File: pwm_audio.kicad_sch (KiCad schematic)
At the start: 16 parts, among them J4 PJ-320D, U7 NC7WZ16P6X

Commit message: Rev.2 (260322)
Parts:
- removed C23: 100n, Capacitor_SMD:C_0402_1005Metric, symbol Device:C
- removed U7: NC7WZ16P6X, Package_TO_SOT_SMD:SOT-363_SC-70-6, symbol 74xGxx:74LVC2G34
- C24, C25: value 100n -> 220n; LCSC (none) -> C21120
- C26, C27: LCSC (none) -> C16133
- D7: renamed from D4; LCSC (none) -> C20615784
- D8: renamed from D5; LCSC (none) -> C20615784
- J4: LCSC (none) -> C431535
- R28, R29: footprint Resistor_SMD:R_0402_1005Metric -> Resistor_SMD:R_0603_1608Metric; LCSC (none) -> C22962
- R30, R31: footprint Resistor_SMD:R_0402_1005Metric -> Resistor_SMD:R_0603_1608Metric; LCSC (none) -> C22775
- R32, R33: footprint Resistor_SMD:R_0402_1005Metric -> Resistor_SMD:R_0603_1608Metric; LCSC (none) -> C25804
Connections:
- net AUDIO_L: now also R28.1
- net AUDIO_R: now also R29.1
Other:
- moved on the sheet: C24, C25, C26, C27, D7, D8, J4, NT1, R28, R29, R30, R31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

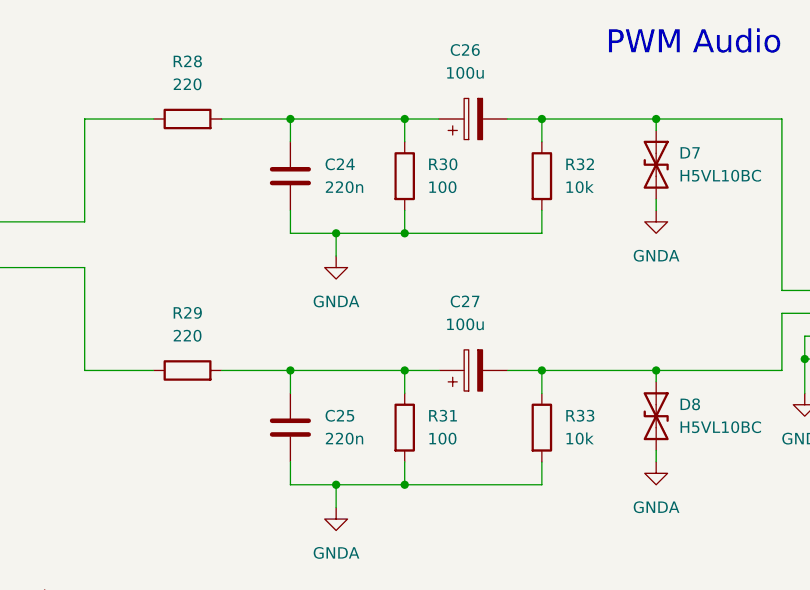
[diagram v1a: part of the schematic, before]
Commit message: Rev. 2B: Change PSRAM package from SOP-8 to USON-8L.
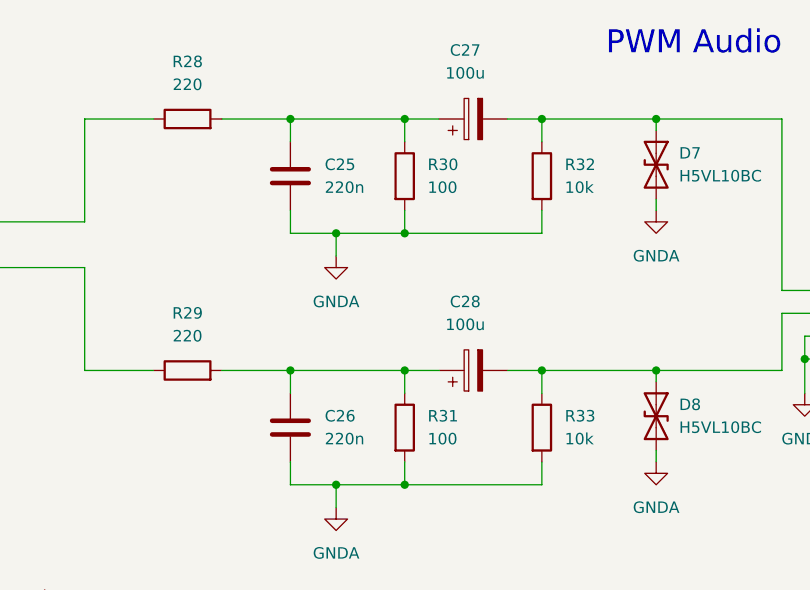
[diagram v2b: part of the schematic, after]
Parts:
- renumbered C24 to C25, C25 to C26, C26 to C27, C27 to C28
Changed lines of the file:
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@@
 	(title_block
 		(title "Harucom-board")
-		(date "2026-03-22")
-		(rev "2")
+		(date "2026-03-23")
+		(rev "2B")
 		(comment 1 "https://github.com/harukasan/harucom-board/")
 		(comment 2 "SPDX-License-Identifier: CERN-OHL-P-2.0")
@@
 		(dnp no)
 		(fields_autoplaced yes)
-		(property "Reference" "C25"
+		(property "Reference" "C26"
 			(at 107.95 106.6799 0)
 			(effects
@@
 			(project ""
 				(path "/0cb5192e-ac62-478f-bacb-beb1b9be1a5b/d71bb1da-6431-4b72-87ca-46892dee63ab"
-					(reference "C25")
+					(reference "C26")
 					(unit 1)
 				)
@@
 		(dnp no)
 		(fields_autoplaced yes)
-		(property "Reference" "C26"
+		(property "Reference" "C27"
 			(at 123.571 66.04 90)
 			(effects
@@
 			(project ""
 				(path "/0cb5192e-ac62-478f-bacb-beb1b9be1a5b/d71bb1da-6431-4b72-87ca-46892dee63ab"
-					(reference "C26")
+					(reference "C27")
 					(unit 1)
 				)
@@
 		(dnp no)
 		(fields_autoplaced yes)
-		(property "Reference" "C27"
+		(property "Reference" "C28"
 			(at 123.571 93.98 90)
 			(effects
@@
 			(project ""
 				(path "/0cb5192e-ac62-478f-bacb-beb1b9be1a5b/d71bb1da-6431-4b72-87ca-46892dee63ab"
-					(reference "C27")
+					(reference "C28")
 					(unit 1)
 				)
@@
 		(dnp no)
 		(fields_autoplaced yes)
-		(property "Reference" "C24"
+		(property "Reference" "C25"
 			(at 107.95 78.7399 0)
 			(effects
@@
 			(project ""
 				(path "/0cb5192e-ac62-478f-bacb-beb1b9be1a5b/d71bb1da-6431-4b72-87ca-46892dee63ab"
-					(reference "C24")
+					(reference "C25")
 					(unit 1)
 				)
